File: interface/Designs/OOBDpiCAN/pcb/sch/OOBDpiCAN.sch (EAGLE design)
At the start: 145 parts, among them IC1 STM32F042CT, IC10 MCP2551SO8, IC11 EEPROM24, IC12 DS3231, IC2 STM32F042CT, IC3 MCP2551SO8, IC4 MCP2551SO8, IC5 ADM3053M, IC6 ADM3053M, IC7 STM32F042CT, IC8 STM32F042CT, IC9 MCP2551SO8, Q1 16MHz, Q2 12MHz

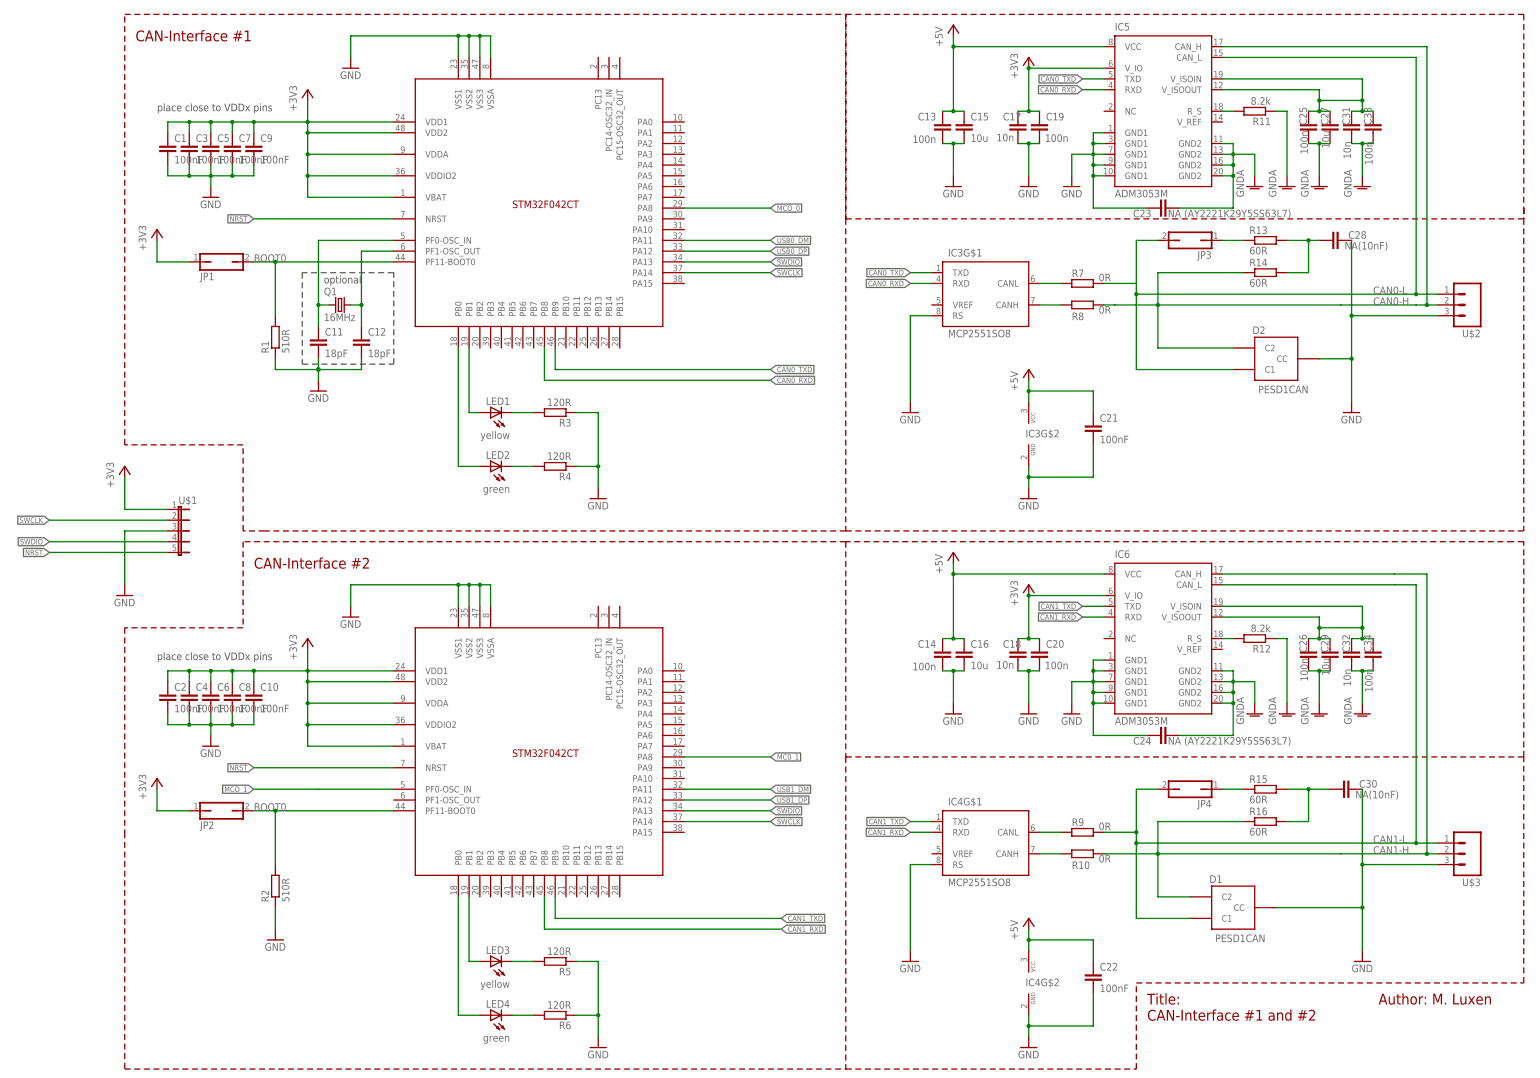
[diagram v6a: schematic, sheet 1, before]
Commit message: - create initial PDF of latest schematics - start placing and routing of CAN-Interfaces
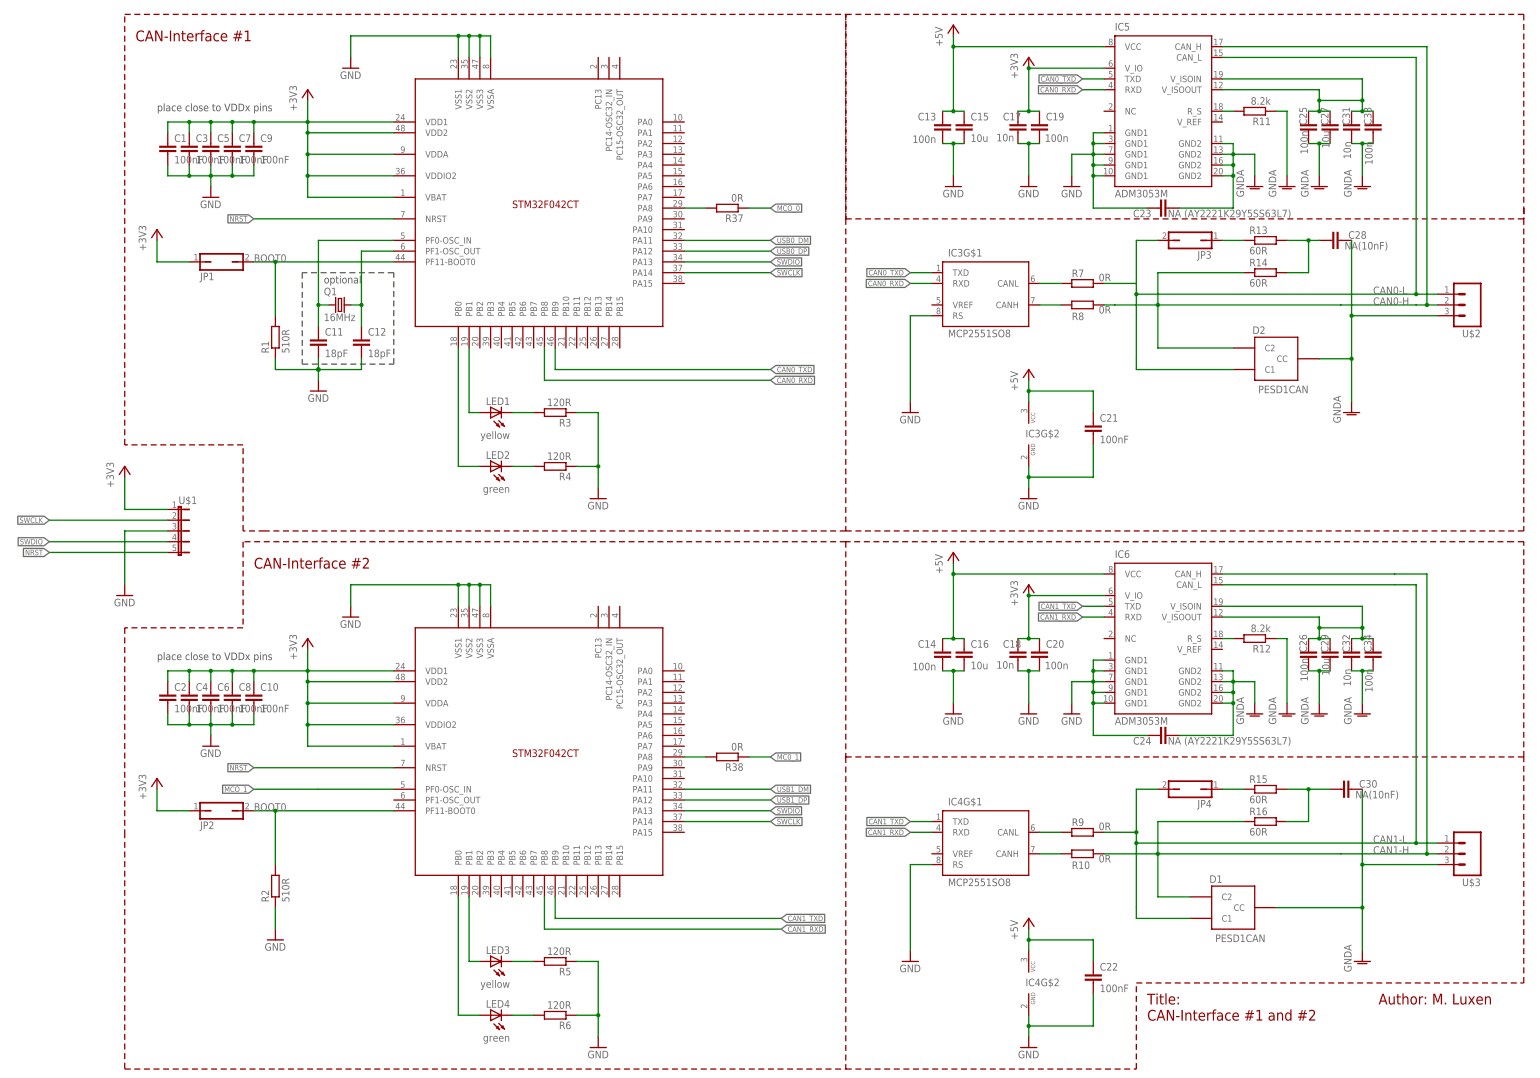
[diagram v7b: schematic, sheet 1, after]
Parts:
- added R37, R38: 0R, rcl:R-EU_R0603
- added R39: 0R, resistor:R-EU_R0603
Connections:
- new net N$43: IC1.PA8, R37.2
- new net N$45: IC2.PA8, R38.2
- new net N$46: IC7.PA8, R39.1
- net GND: no longer C28.2, C30.2, D1.CC, D2.CC, U$2.4, U$3.4
- net GNDA: now also C28.2, C30.2, D1.CC, D2.CC, U$2.4, U$3.4
- net MC0_1: now also R38.1; no longer IC2.PA8
- net MCO_0: now also R37.1; no longer IC1.PA8
- net MCO_2: now also R39.2; no longer IC7.PA8
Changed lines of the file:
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@@
 <setting verticaltext="up"/>
 </settings>
-<grid distance="0.1" unitdist="inch" unit="inch" style="lines" multiple="1" display="no" altdistance="0.01" altunitdist="inch" altunit="inch"/>
+<grid distance="0.1" unitdist="inch" unit="inch" style="lines" multiple="1" display="yes" altdistance="0.01" altunitdist="inch" altunit="inch"/>
 <layers>
 <layer number="1" name="Top" color="4" fill="1" visible="no" active="no"/>
@@
 <part name="GND27" library="supply1" deviceset="GND" device=""/>
 <part name="U$3" library="SparkFun-Connectors" deviceset="M03" device=""/>
-<part name="GND28" library="supply1" deviceset="GND" device=""/>
 <part name="LED4" library="led" deviceset="LED" device="CHIPLED_0805" value="green"/>
 <part name="LED3" library="led" deviceset="LED" device="CHIPLED_0805" value="yellow"/>
@@
 <part name="JP3" library="jumper" deviceset="JP1Q" device=""/>
 <part name="U$2" library="SparkFun-Connectors" deviceset="M03" device=""/>
-<part name="GND21" library="supply1" deviceset="GND" device=""/>
 <part name="R14" library="resistor" deviceset="R-EU_" device="R0603" value="60R"/>
 <part name="C28" library="resistor" deviceset="C-EU" device="C0603" value="NA(10nF)"/>
@@
 <part name="C24" library="rcl" deviceset="C-EU" device="075-032X103" value="NA (AY2221K29Y5SS63L7)"/>
 <part name="C23" library="rcl" deviceset="C-EU" device="075-032X103" value="NA (AY2221K29Y5SS63L7)"/>
+<part name="R37" library="rcl" deviceset="R-EU_" device="R0603" value="0R"/>
+<part name="R38" library="rcl" deviceset="R-EU_" device="R0603" value="0R"/>
+<part name="R39" library="resistor" deviceset="R-EU_" device="R0603" value="0R"/>
+<part name="GND45" library="supply1" deviceset="GNDA" device=""/>
+<part name="GND28" library="supply1" deviceset="GNDA" device=""/>
 </parts>
 <sheets>
@@
 <instance part="GND27" gate="1" x="68.58" y="81.28"/>
 <instance part="U$3" gate="G$1" x="365.76" y="55.88" rot="R180"/>
-<instance part="GND28" gate="1" x="340.36" y="30.48"/>
 <instance part="LED4" gate="G$1" x="134.62" y="17.78" smashed="yes" rot="R90">
 <attribute name="NAME" x="139.192" y="21.336" size="1.778" layer="95" rot="R180"/>
@@
 <instance part="JP3" gate="A" x="299.72" y="200.66" rot="R90"/>
 <instance part="U$2" gate="G$1" x="365.76" y="185.42" rot="R180"/>
-<instance part="GND21" gate="1" x="337.82" y="160.02"/>
 <instance part="R14" gate="G$1" x="317.5" y="193.04"/>
 <instance part="C28" gate="G$1" x="332.74" y="200.66" smashed="yes" rot="R90">
@@
 <attribute name="VALUE" x="323.596" y="207.899" size="1.778" layer="96" rot="R180"/>
 </instance>
+<instance part="R37" gate="G$1" x="190.5" y="208.28" rot="R180"/>
+<instance part="R38" gate="G$1" x="190.5" y="78.74" rot="R180"/>
+<instance part="GND45" gate="1" x="340.36" y="30.48"/>
+<instance part="GND28" gate="1" x="337.82" y="160.02"/>
 </instances>
 <busses>
@@
 </segment>
 <segment>
-<pinref part="GND28" gate="1" pin="GND"/>
-<wire x1="340.36" y1="33.02" x2="340.36" y2="43.18" width="0.1524" layer="91"/>
-<pinref part="U$3" gate="G$1" pin="4"/>
-<wire x1="340.36" y1="43.18" x2="340.36" y2="53.34" width="0.1524" layer="91"/>
-<wire x1="340.36" y1="53.34" x2="358.14" y2="53.34" width="0.1524" layer="91"/>
-<pinref part="C30" gate="G$1" pin="2"/>
-<wire x1="340.36" y1="53.34" x2="340.36" y2="71.12" width="0.1524" layer="91"/>
-<junction x="340.36" y="53.34"/>
-<pinref part="D1" gate="G$1" pin="CC"/>
-<wire x1="320.04" y1="43.18" x2="340.36" y2="43.18" width="0.1524" layer="91"/>
-<junction x="340.36" y="43.18"/>
-</segment>
-<segment>
 <pinref part="GND29" gate="1" pin="GND"/>
 <wire x1="160.02" y1="12.7" x2="160.02" y2="17.78" width="0.1524" layer="91"/>
@@
 <pinref part="GND19" gate="1" pin="GND"/>
 <wire x1="233.68" y1="182.88" x2="233.68" y2="162.56" width="0.1524" layer="91"/>
-</segment>
-<segment>
-<pinref part="GND21" gate="1" pin="GND"/>
-<wire x1="337.82" y1="162.56" x2="337.82" y2="172.72" width="0.1524" layer="91"/>
-<pinref part="U$2" gate="G$1" pin="4"/>
-<wire x1="337.82" y1="172.72" x2="337.82" y2="182.88" width="0.1524" layer="91"/>
-<wire x1="337.82" y1="182.88" x2="358.14" y2="182.88" width="0.1524" layer="91"/>
-<pinref part="C28" gate="G$1" pin="2"/>
-<wire x1="337.82" y1="182.88" x2="337.82" y2="200.66" width="0.1524" layer="91"/>
-<junction x="337.82" y="182.88"/>
-<pinref part="D2" gate="G$1" pin="CC"/>
-<wire x1="330.2" y1="172.72" x2="337.82" y2="172.72" width="0.1524" layer="91"/>
-<junction x="337.82" y="172.72"/>
 </segment>
 <segment>
@@
 <net name="MC0_1" class="0">
 <segment>
-<pinref part="IC2" gate="G$1" pin="PA8"/>
-<wire x1="180.34" y1="78.74" x2="200.66" y2="78.74" width="0.1524" layer="91"/>
 <label x="200.66" y="78.74" size="1.27" layer="95" xref="yes"/>
+<pinref part="R38" gate="G$1" pin="1"/>
+<wire x1="195.58" y1="78.74" x2="200.66" y2="78.74" width="0.1524" layer="91"/>
 </segment>
 </net>
@@
 <net name="MCO_0" class="0">
 <segment>
-<pinref part="IC1" gate="G$1" pin="PA8"/>
-<wire x1="180.34" y1="208.28" x2="200.66" y2="208.28" width="0.1524" layer="91"/>
 <label x="200.66" y="208.28" size="1.27" layer="95" xref="yes"/>
+<pinref part="R37" gate="G$1" pin="1"/>
+<wire x1="195.58" y1="208.28" x2="200.66" y2="208.28" width="0.1524" layer="91"/>
 </segment>
 </net>
@@
 <junction x="340.36" y="99.06"/>
 </segment>
+<segment>
+<wire x1="340.36" y1="33.02" x2="340.36" y2="43.18" width="0.1524" layer="91"/>
+<pinref part="U$3" gate="G$1" pin="4"/>
+<wire x1="340.36" y1="43.18" x2="340.36" y2="53.34" width="0.1524" layer="91"/>
+<wire x1="340.36" y1="53.34" x2="358.14" y2="53.34" width="0.1524" layer="91"/>
+<pinref part="C30" gate="G$1" pin="2"/>
+<wire x1="340.36" y1="53.34" x2="340.36" y2="71.12" width="0.1524" layer="91"/>
+<junction x="340.36" y="53.34"/>
+<pinref part="D1" gate="G$1" pin="CC"/>
+<wire x1="320.04" y1="43.18" x2="340.36" y2="43.18" width="0.1524" layer="91"/>
+<junction x="340.36" y="43.18"/>
+<pinref part="GND45" gate="1" pin="GNDA"/>
+</segment>
+<segment>
+<wire x1="337.82" y1="162.56" x2="337.82" y2="172.72" width="0.1524" layer="91"/>
+<pinref part="U$2" gate="G$1" pin="4"/>
+<wire x1="337.82" y1="172.72" x2="337.82" y2="182.88" width="0.1524" layer="91"/>
+<wire x1="337.82" y1="182.88" x2="358.14" y2="182.88" width="0.1524" layer="91"/>
+<pinref part="C28" gate="G$1" pin="2"/>
+<wire x1="337.82" y1="182.88" x2="337.82" y2="200.66" width="0.1524" layer="91"/>
+<junction x="337.82" y="182.88"/>
+<pinref part="D2" gate="G$1" pin="CC"/>
+<wire x1="330.2" y1="172.72" x2="337.82" y2="172.72" width="0.1524" layer="91"/>
+<junction x="337.82" y="172.72"/>
+<pinref part="GND28" gate="1" pin="GNDA"/>
+</segment>
 </net>
 <net name="N$1" class="0">
@@
 <pinref part="IC3" gate="G$1" pin="CANH"/>
 <wire x1="269.24" y1="185.42" x2="264.16" y2="185.42" width="0.1524" layer="91"/>
+</segment>
+</net>
+<net name="N$43" class="0">
+<segment>
+<pinref part="IC1" gate="G$1" pin="PA8"/>
+<pinref part="R37" gate="G$1" pin="2"/>
+<wire x1="180.34" y1="208.28" x2="185.42" y2="208.28" width="0.1524" layer="91"/>
+</segment>
+</net>
+<net name="N$45" class="0">
+<segment>
+<pinref part="IC2" gate="G$1" pin="PA8"/>
+<pinref part="R38" gate="G$1" pin="2"/>
+<wire x1="180.34" y1="78.74" x2="185.42" y2="78.74" width="0.1524" layer="91"/>
 </segment>
 </net>
@@
 <attribute name="VALUE" x="317.5" y="36.83" size="1.778" layer="96" rot="R180"/>
 </instance>
+<instance part="R39" gate="G$1" x="190.5" y="208.28"/>
 </instances>
 <busses>
@@
 <net name="MCO_2" class="0">
 <segment>
-<pinref part="IC7" gate="G$1" pin="PA8"/>
-<wire x1="180.34" y1="208.28" x2="200.66" y2="208.28" width="0.1524" layer="91"/>
 <label x="200.66" y="208.28" size="1.27" layer="95" xref="yes"/>
+<pinref part="R39" gate="G$1" pin="2"/>
+<wire x1="195.58" y1="208.28" x2="200.66" y2="208.28" width="0.1524" layer="91"/>
 </segment>
 <segment>
@@
 </segment>
 </net>
+<net name="N$46" class="0">
+<segment>
+<pinref part="IC7" gate="G$1" pin="PA8"/>
+<pinref part="R39" gate="G$1" pin="1"/>
+<wire x1="180.34" y1="208.28" x2="185.42" y2="208.28" width="0.1524" layer="91"/>
+</segment>
+</net>

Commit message: add latest modifications to OOBD schematics
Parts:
- C17, C18: value 10n -> 10u; device rcl:C-EUC0603K -> rcl:C-EUC0805K
- R11, R12: value 8.2k -> 8k2
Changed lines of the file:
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@@
 <setting verticaltext="up"/>
 </settings>
-<grid distance="0.1" unitdist="inch" unit="inch" style="lines" multiple="1" display="yes" altdistance="0.01" altunitdist="inch" altunit="inch"/>
+<grid distance="0.1" unitdist="inch" unit="inch" style="lines" multiple="1" display="no" altdistance="0.01" altunitdist="inch" altunit="inch"/>
 <layers>
 <layer number="1" name="Top" color="4" fill="1" visible="no" active="no"/>
@@
 <part name="P+19" library="supply1" deviceset="+5V" device=""/>
 <part name="IC5" library="ADM3053" deviceset="ADM3053" device="M"/>
-<part name="C17" library="rcl" deviceset="C-EU" device="C0603K" value="10n"/>
+<part name="C17" library="rcl" deviceset="C-EU" device="C0805K" value="10u"/>
 <part name="C19" library="rcl" deviceset="C-EU" device="C0603K" value="100n"/>
 <part name="GND52" library="supply1" deviceset="GND" device=""/>
@@
 <part name="+3V14" library="supply1" deviceset="+3V3" device=""/>
 <part name="GND56" library="supply1" deviceset="GNDA" device=""/>
-<part name="R11" library="rcl" deviceset="R-EU_" device="R0603" value="8.2k"/>
+<part name="R11" library="rcl" deviceset="R-EU_" device="R0603" value="8k2"/>
 <part name="GND57" library="supply1" deviceset="GNDA" device=""/>
 <part name="GND58" library="supply1" deviceset="GNDA" device=""/>
@@
 <part name="P+2" library="supply1" deviceset="+5V" device=""/>
 <part name="IC6" library="ADM3053" deviceset="ADM3053" device="M"/>
-<part name="C18" library="rcl" deviceset="C-EU" device="C0603K" value="10n"/>
+<part name="C18" library="rcl" deviceset="C-EU" device="C0805K" value="10u"/>
 <part name="C20" library="rcl" deviceset="C-EU" device="C0603K" value="100n"/>
 <part name="GND10" library="supply1" deviceset="GND" device=""/>
@@
 <part name="+3V15" library="supply1" deviceset="+3V3" device=""/>
 <part name="GND39" library="supply1" deviceset="GNDA" device=""/>
-<part name="R12" library="rcl" deviceset="R-EU_" device="R0603" value="8.2k"/>
+<part name="R12" library="rcl" deviceset="R-EU_" device="R0603" value="8k2"/>
 <part name="GND40" library="supply1" deviceset="GNDA" device=""/>
 <part name="GND41" library="supply1" deviceset="GNDA" device=""/>
